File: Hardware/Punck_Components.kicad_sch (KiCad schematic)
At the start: 128 parts, among them J1 Conn_01x08_Male, J2 Conn_01x08_Male, J3 Conn_01x08_Male, J4 Conn_01x08_Male, J5 SWD_Header, J6 USB_B_Micro, J7 Eurorack_10_pin_power, Q1 MMBT3904, U1 MCP6004, U10 PCM5100APW, U11 LM2675M-5, U12 LD1117-3.3-4Tab, U2 TL074, U3 MCP6004, U5 W25Q128JVS, U6 STM32H743ZITx, U7 TL072, Y1 8MHz 20pF

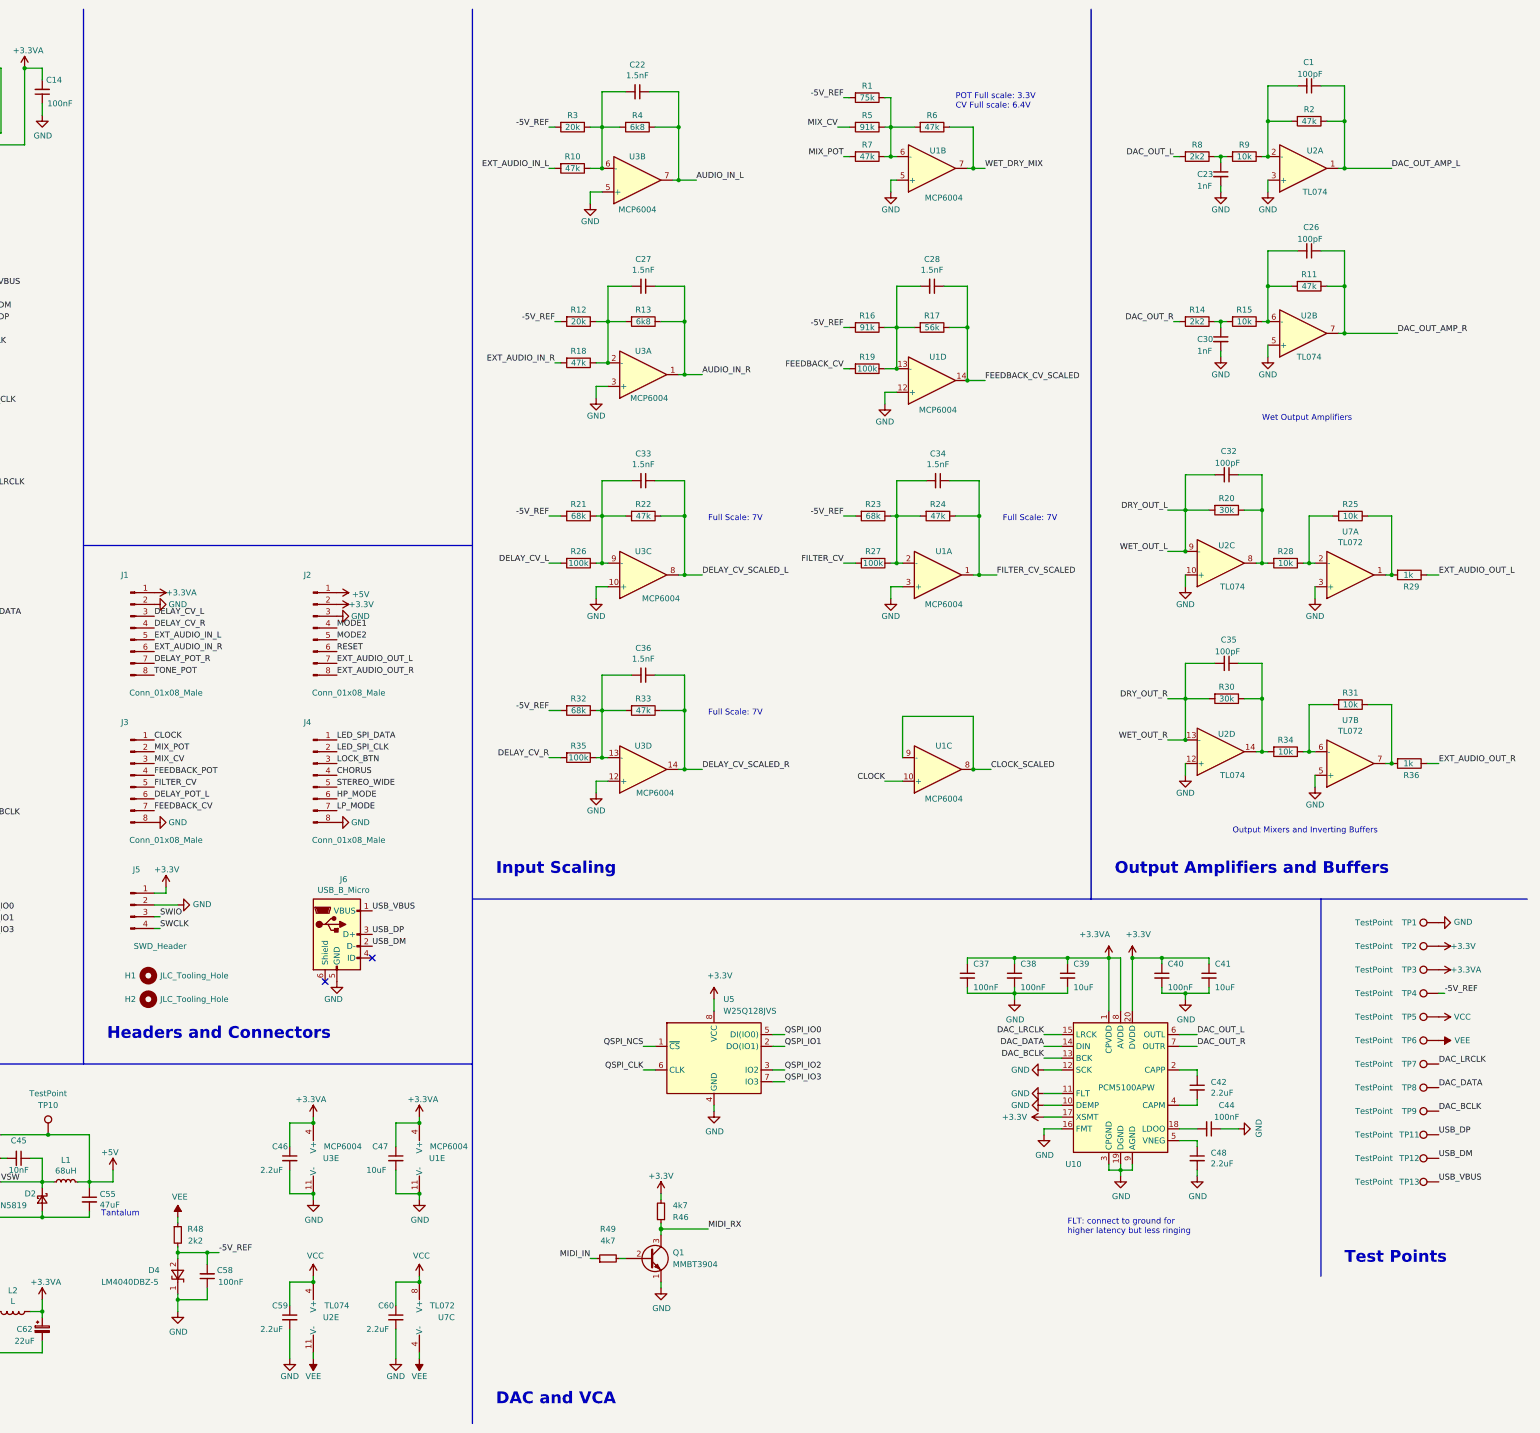
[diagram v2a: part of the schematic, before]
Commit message: Added better handling for problems with flash device
+ temporarily lowered the speed of the QSPI flash as demo rig was glitching
+ added a diagnostic to get Flash manufacturer and device ID
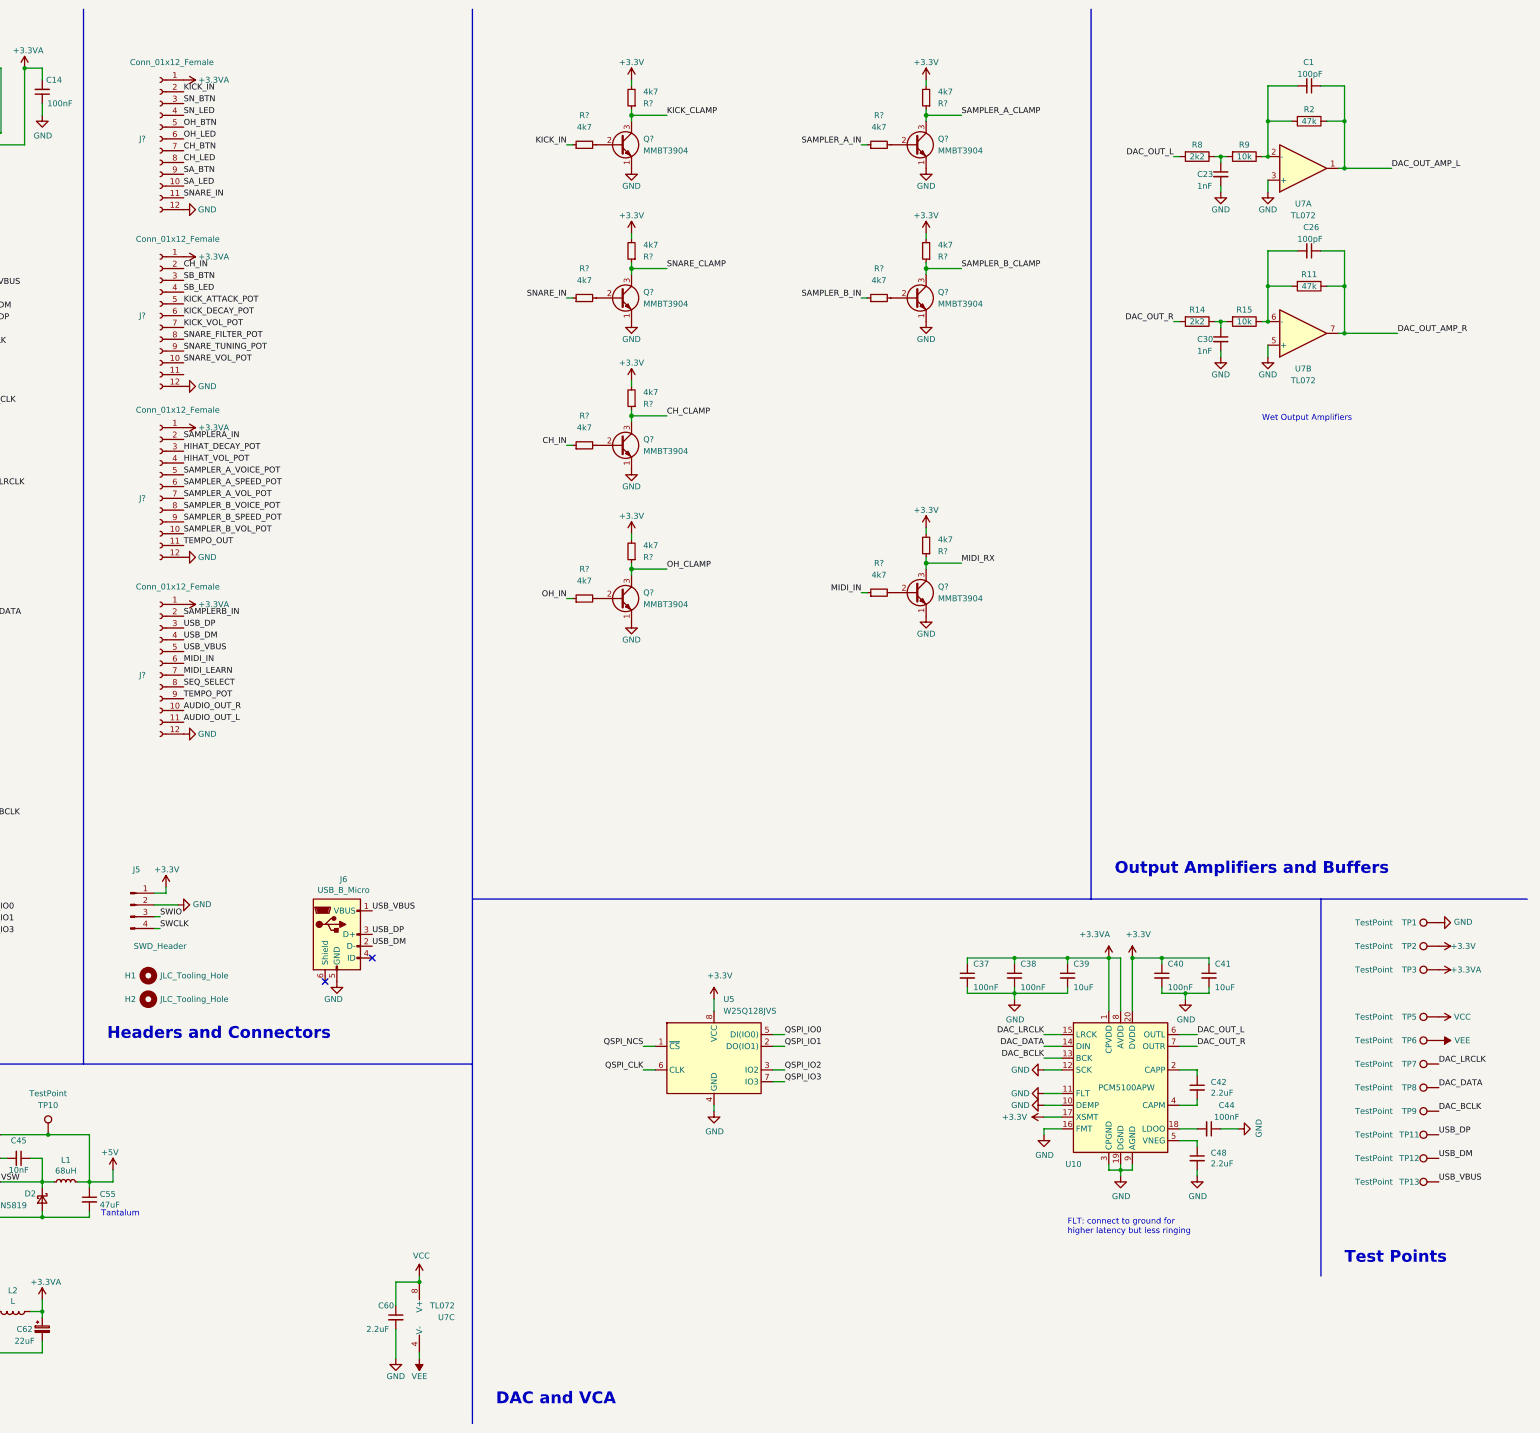
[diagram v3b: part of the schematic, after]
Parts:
- removed C22, C27, C28, C33, C34, C36: 1.5nF, Capacitors_SMD:C_0603_HandSoldering, symbol Device:C_Small
- removed C32, C35: 100pF, Capacitors_SMD:C_0603_HandSoldering, symbol Device:C_Small
- removed C46, C59: 2.2uF, Capacitors_SMD:C_0603_HandSoldering, symbol Device:C_Small
- removed C47: 10uF, Capacitors_SMD:C_0805, symbol Device:C_Small
- removed C58: 100nF, Capacitors_SMD:C_0603_HandSoldering, symbol Device:C_Small
- removed D4: LM4040DBZ-5, TO_SOT_Packages_SMD:SOT-23, symbol Reference_Voltage:LM4040DBZ-10
- removed J1, J2, J3, J4: Conn_01x08_Male, Pin_Headers:Pin_Header_Straight_1x08_Pitch2.54mm, symbol Connector:Conn_01x08_Male
- removed Q1: MMBT3904, Package_TO_SOT_THT:TO-92_Inline, symbol Transistor_BJT:2N3904
- removed R1: 75k, Resistors_SMD:R_0603_HandSoldering, symbol Device:R
- removed R10, R18, R22, R24, R33, R6, R7: 47k, Resistors_SMD:R_0603_HandSoldering, symbol Device:R
- removed R12, R3: 20k, Resistors_SMD:R_0603_HandSoldering, symbol Device:R
- removed R13, R4: 6k8, Resistors_SMD:R_0603_HandSoldering, symbol Device:R
- removed R16, R5: 91k, Resistors_SMD:R_0603_HandSoldering, symbol Device:R
- removed R17: 56k, Resistors_SMD:R_0603_HandSoldering, symbol Device:R
- removed R19, R26, R27, R35: 100k, Resistors_SMD:R_0603_HandSoldering, symbol Device:R
- removed R20, R30: 30k, Resistors_SMD:R_0603_HandSoldering, symbol Device:R
- removed R21, R23, R32: 68k, Resistors_SMD:R_0603_HandSoldering, symbol Device:R
- removed R25, R28, R31, R34: 10k, Resistors_SMD:R_0603_HandSoldering, symbol Device:R
- removed R29, R36: 1k, Resistors_SMD:R_0603_HandSoldering, symbol Device:R
- removed R46, R49: 4k7, Resistor_SMD:R_0603_1608Metric, symbol Device:R_Small
- removed R48: 2k2, Resistors_SMD:R_0603_HandSoldering, symbol Device:R_Small
- removed TP4: TestPoint, Custom_Footprints:1.3mm_Test_Point, symbol Connector:TestPoint
- removed U1, U3: MCP6004, SMD_Packages:SOIC-14_N, symbol Amplifier_Operational:MCP6004
- removed U2: TL074, SMD_Packages:SOIC-14_N, symbol Amplifier_Operational:TL074
- added J? (x4): Conn_01x12_Female, Connector_PinHeader_2.54mm:PinHeader_1x12_P2.54mm_Vertical, symbol Connector:Conn_01x12_Female
- added Q? (x7): MMBT3904, Package_TO_SOT_THT:TO-92_Inline, symbol Transistor_BJT:2N3904
- added R? (x14): 4k7, Resistor_SMD:R_0603_1608Metric, symbol Device:R_Small
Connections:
- net +3.3VA: now also J?.1 (Pin_1), J?.1 (Pin_1), J?.1 (Pin_1), J?.1 (Pin_1)
- net +3V3: now also R?.2, R?.2, R?.2, R?.2, R?.2, R?.2, R?.2
- net DAC_OUT_AMP_L: now also U7.1
- net DAC_OUT_AMP_R: now also U7.7
- net GND: now also J?.12 (Pin_12), J?.12 (Pin_12), J?.12 (Pin_12), J?.12 (Pin_12), Q?.1 (E), Q?.1 (E), Q?.1 (E), Q?.1 (E), Q?.1 (E), Q?.1 (E), Q?.1 (E)
- net MIDI_IN: now also J?.6 (Pin_6), R?.1
- net MIDI_RX: now also Q?.3 (C), R?.1
- net USB_DM: now also J?.4 (Pin_4)
- net USB_DP: now also J?.3 (Pin_3)
- net USB_VBUS: now also J?.5 (Pin_5)
- net at U7.2 (-): now also C1.2, R2.2, R9.1
- net at U7.6 (-): now also C26.2, R11.2, R15.1
- new net: Q?.2 (B), R?.2 (x7)
- new net AUDIO_OUT_L: J?.11 (Pin_11)
- new net AUDIO_OUT_R: J?.10 (Pin_10)
- new net CH_BTN: J?.7 (Pin_7)
- new net CH_CLAMP: Q?.3 (C), R?.1
- new net CH_IN: J?.2 (Pin_2), R?.1
- new net CH_LED: J?.8 (Pin_8)
- new net HIHAT_DECAY_POT: J?.3 (Pin_3)
- new net HIHAT_VOL_POT: J?.4 (Pin_4)
- new net KICK_ATTACK_POT: J?.5 (Pin_5)
- new net KICK_CLAMP: Q?.3 (C), R?.1
- new net KICK_DECAY_POT: J?.6 (Pin_6)
- new net KICK_IN: J?.2 (Pin_2), R?.1
- new net KICK_VOL_POT: J?.7 (Pin_7)
- new net MIDI_LEARN: J?.7 (Pin_7)
- new net OH_BTN: J?.5 (Pin_5)
- new net OH_CLAMP: Q?.3 (C), R?.1
- new net OH_IN: R?.1
- new net OH_LED: J?.6 (Pin_6)
- new net SAMPLERA_IN: J?.2 (Pin_2)
- new net SAMPLERB_IN: J?.2 (Pin_2)
- new net SAMPLER_A_CLAMP: Q?.3 (C), R?.1
- new net SAMPLER_A_IN: R?.1
- new net SAMPLER_A_SPEED_POT: J?.6 (Pin_6)
- new net SAMPLER_A_VOICE_POT: J?.5 (Pin_5)
- new net SAMPLER_A_VOL_POT: J?.7 (Pin_7)
- new net SAMPLER_B_CLAMP: Q?.3 (C), R?.1
- new net SAMPLER_B_IN: R?.1
- new net SAMPLER_B_SPEED_POT: J?.9 (Pin_9)
- new net SAMPLER_B_VOICE_POT: J?.8 (Pin_8)
- new net SAMPLER_B_VOL_POT: J?.10 (Pin_10)
- new net SA_BTN: J?.9 (Pin_9)
- new net SA_LED: J?.10 (Pin_10)
- new net SB_BTN: J?.3 (Pin_3)
- new net SB_LED: J?.4 (Pin_4)
- new net SEQ_SELECT: J?.8 (Pin_8)
- new net SNARE_CLAMP: Q?.3 (C), R?.1
- new net SNARE_FILTER_POT: J?.8 (Pin_8)
- new net SNARE_IN: J?.11 (Pin_11), R?.1
- new net SNARE_TUNING_POT: J?.9 (Pin_9)
- new net SNARE_VOL_POT: J?.10 (Pin_10)
- new net SN_BTN: J?.3 (Pin_3)
- new net SN_LED: J?.4 (Pin_4)
- new net TEMPO_OUT: J?.11 (Pin_11)
- new net TEMPO_POT: J?.9 (Pin_9)
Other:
- note removed: "Full Scale: 7V"
- note removed: "Input Scaling"
- note removed: "Output Mixers and Inverting Buffers"
- note removed: "POT Full scale: 3.3V CV Full scale: 6.4V"
- moved on the sheet: U7A, U7B

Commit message: Started component PCB
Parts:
- added C27, C36: (no value), symbol Device:C_Small
- added R16, R23, R24, R25, R26, R27, R28, R8: (no value), symbol Device:R_Small
- added U6: (no value), symbol Memory_Flash:W25Q128JVS
- C1: value 100pF -> (none); footprint Capacitors_SMD:C_0603_HandSoldering -> (none)
- C10, C11, C12, C13, C14, C2, C3, C4, C5, C6, C7, C8, C9: value 100nF -> (none); footprint Capacitors_SMD:C_0603_HandSoldering -> (none)
- C15: renamed from C23; value 1nF -> (none); footprint Capacitors_SMD:C_0603_HandSoldering -> (none)
- C16: renamed from C24; value 2.2uF -> (none); footprint Capacitors_SMD:C_0603_HandSoldering -> (none)
- C17: renamed from C25; value 2.2uF -> (none); footprint Capacitors_SMD:C_0603_HandSoldering -> (none)
- C18: renamed from C26; value 100pF -> (none); footprint Capacitors_SMD:C_0603_HandSoldering -> (none)
- C19: renamed from C29; value 30pF -> (none); footprint Capacitors_SMD:C_0603_HandSoldering -> (none)
- C20: renamed from C30; value 1nF -> (none); footprint Capacitors_SMD:C_0603_HandSoldering -> (none)
- C21: renamed from C31; value 30pF -> (none); footprint Capacitors_SMD:C_0603_HandSoldering -> (none)
- C22: renamed from C37; value 100nF -> (none); footprint Capacitors_SMD:C_0603_HandSoldering -> (none)
- C23: renamed from C38; value 100nF -> (none); footprint Capacitors_SMD:C_0603_HandSoldering -> (none)
- C24: renamed from C39; value 10uF -> (none); footprint Capacitors_SMD:C_0805 -> (none)
- C25: renamed from C40; value 100nF -> (none); footprint Capacitors_SMD:C_0603_HandSoldering -> (none)
- C26: renamed from C41; value 10uF -> (none); footprint Capacitors_SMD:C_0805 -> (none)
- C28: renamed from C42; value 2.2uF -> (none); footprint Capacitors_SMD:C_0603_HandSoldering -> (none)
- C29: renamed from C43; value 47uF -> (none); footprint Capacitors_SMD:CP_Elec_5x5.8 -> (none); symbol Device:CP -> Device:C_Polarized_Small
- C30: renamed from C44; value 100nF -> (none); footprint Capacitors_SMD:C_0603_HandSoldering -> (none)
- C31: renamed from C45; value 10nF -> (none); footprint Capacitors_SMD:C_0603_HandSoldering -> (none)
- C32: renamed from C48; value 2.2uF -> (none); footprint Capacitors_SMD:C_0603_HandSoldering -> (none)
- C33: renamed from C53; value 100nF -> (none); footprint Capacitors_SMD:C_0603_HandSoldering -> (none)
- C34: renamed from C54; value 22uF -> (none); footprint Capacitors_SMD:C_1210 -> (none)
- C35: renamed from C55; value 47uF -> (none); footprint Capacitors_SMD:C_1210 -> (none)
- C37: renamed from C57; value 22uF -> (none); footprint Capacitors_SMD:CP_Elec_4x5.8 -> (none); symbol Device:CP -> Device:C_Polarized_Small
- C38: renamed from C60; value 2.2uF -> (none); footprint Capacitors_SMD:C_0603_HandSoldering -> (none)
- C39: renamed from C61; value 47uF -> (none); footprint Capacitors_SMD:CP_Elec_5x5.8 -> (none); symbol Device:CP_Small -> Device:C_Polarized_Small
- C40: renamed from C62; value 22uF -> (none); footprint Capacitors_SMD:CP_Elec_4x5.8 -> (none); symbol Device:CP_Small -> Device:C_Polarized_Small
- D1, D2, D3: value 1N5819 -> (none); footprint Diodes_SMD:D_SOD-123 -> (none)
- H1, H2: value JLC_Tooling_Hole -> (none); footprint Custom_Footprints:JLC_SMT_Tooling_Hole -> (none)
- J1, J2, J3, J4: renamed from J?; value Conn_01x12_Female -> (none); footprint Connector_PinHeader_2.54mm:PinHeader_1x12_P2.54mm_Vertical -> (none)
- J5: value SWD_Header -> (none); footprint Custom_Footprints:SWD_header -> (none)
- J6: value USB_B_Micro -> (none); footprint Custom_Footprints:USB_Micro-B_Amphenol -> (none)
- J7: value Eurorack_10_pin_power -> (none); footprint Custom_Footprints:Eurorack_10_pin_header -> (none)
- L1: value 68uH -> (none); footprint Custom_Footprints:TDK_Inductor_6.9x7.2 -> (none)
- L2: value L -> (none); footprint Inductors_SMD:L_0805_HandSoldering -> (none)
- Q1, Q2, Q3, Q4, Q5, Q6, Q7: renamed from Q?; value MMBT3904 -> (none); footprint Package_TO_SOT_THT:TO-92_Inline -> (none)
- R1, R10, R12, R13, R17, R18, R19, R2, R20, R21, R22, R4, R5, R9: renamed from R?; value 4k7 -> (none); footprint Resistor_SMD:R_0603_1608Metric -> (none)
- R11: value 47k -> (none); footprint Resistors_SMD:R_0603_HandSoldering -> (none)
- R14: value 2k2 -> (none); footprint Resistors_SMD:R_0603_HandSoldering -> (none)
- R15: value 10k -> (none); footprint Resistors_SMD:R_0603_HandSoldering -> (none)
- R3: renamed from R2; value 47k -> (none); footprint Resistors_SMD:R_0603_HandSoldering -> (none)
- R6: renamed from R8; value 2k2 -> (none); footprint Resistors_SMD:R_0603_HandSoldering -> (none)
- R7: renamed from R9; value 10k -> (none); footprint Resistors_SMD:R_0603_HandSoldering -> (none)
- TP1, TP2, TP3: value TestPoint -> (none); footprint Custom_Footprints:1.3mm_Test_Point -> (none)
- TP10: renamed from TP11; value TestPoint -> (none); footprint Measurement_Points:Measurement_Point_Square-SMD-Pad_Small -> (none)
- TP11: renamed from TP12; value TestPoint -> (none); footprint Measurement_Points:Measurement_Point_Square-SMD-Pad_Small -> (none)
- TP12: renamed from TP13; value TestPoint -> (none); footprint Measurement_Points:Measurement_Point_Square-SMD-Pad_Small -> (none)
- TP4: renamed from TP5; value TestPoint -> (none); footprint Custom_Footprints:1.3mm_Test_Point -> (none)
- TP5: renamed from TP6; value TestPoint -> (none); footprint Custom_Footprints:1.3mm_Test_Point -> (none)
- TP6: renamed from TP7; value TestPoint -> (none); footprint Measurement_Points:Measurement_Point_Square-SMD-Pad_Small -> (none)
- TP7: renamed from TP8; value TestPoint -> (none); footprint Measurement_Points:Measurement_Point_Square-SMD-Pad_Small -> (none)
- TP8: renamed from TP9; value TestPoint -> (none); footprint Measurement_Points:Measurement_Point_Square-SMD-Pad_Small -> (none)
- TP9: renamed from TP10; value TestPoint -> (none); footprint Measurement_Points:Measurement_Point_Square-SMD-Pad_Small -> (none)
- U1: renamed from U7; value TL072 -> (none); footprint Housings_SOIC:SOIC-8_3.9x4.9mm_Pitch1.27mm -> (none)
- U2: renamed from U6; value STM32H743ZITx -> (none); footprint Package_QFP:LQFP-144_20x20mm_P0.5mm -> (none)
- U3: renamed from U5; value W25Q128JVS -> (none); footprint Package_SO:SOIC-8_5.23x5.23mm_P1.27mm -> (none)
- U4: renamed from U10; value PCM5100APW -> (none); footprint Custom_Footprints:SSOP-20_4.4x6.5mm_Pitch0.65mm_Round_Pads -> (none)
- U5: renamed from U11; value LM2675M-5 -> (none); footprint Housings_SOIC:SOIC-8_3.9x4.9mm_Pitch1.27mm -> (none)
- U7: renamed from U12; value LD1117-3.3-4Tab -> (none); footprint TO_SOT_Packages_SMD:SOT-223-3_TabPin2 -> (none)
- Y1: value 8MHz 20pF -> (none); footprint Crystals:Crystal_SMD_5032-2pin_5.0x3.2mm_HandSoldering -> (none)
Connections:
- net +3.3VA: no longer J2.1 (Pin_1), J3.1 (Pin_1)
- net +3V3: now also C27.1, C36.1, U6.8 (VCC)
- net AUDIO_OUT_L: now also R8.2
- net AUDIO_OUT_R: now also R16.2
- net CH_BTN: now also U2.13 (PF3)
- net CH_CLAMP: now also U2.136 (PB6)
- net CH_IN: now also J2.3 (Pin_3); no longer J2.2 (Pin_2)
- net CH_LED: now also R25.1
- net DAC_BCLK: now also U2.74 (PB13); no longer U2.117 (PD3)
- net DAC_DATA: now also U2.76 (PB15); no longer U2.29 (PC3_C)
- net GND: now also C27.2, C36.2, U6.4 (GND)
- net HIHAT_DECAY_POT: now also U2.46 (PB0)
- net HIHAT_VOL_POT: now also U2.47 (PB1)
- net KICK_ATTACK_POT: now also J2.6 (Pin_6), U2.34 (PA0); no longer J2.5 (Pin_5)
- net KICK_CLAMP: now also U2.137 (PB7)
- net KICK_DECAY_POT: now also J2.7 (Pin_7), U2.35 (PA1); no longer J2.6 (Pin_6)
- net KICK_VOL_POT: now also J2.8 (Pin_8), U2.36 (PA2); no longer J2.7 (Pin_7)
- net MIDI_LEARN: now also U2.67 (PE14)
- net OH_BTN: now also U2.12 (PF2)
- net OH_CLAMP: now also U2.93 (PG8)
- net OH_IN: now also J3.1 (Pin_1)
- net OH_LED: now also R26.1
- net QSPI_CLK: now also U6.6 (CLK)
- net QSPI_IO2: no longer U3.3 (IO2)
- net SAMPLER_A_CLAMP: now also U2.125 (PG10)
- net SAMPLER_A_SPEED_POT: now also U2.27 (PC1)
- net SAMPLER_A_VOICE_POT: now also U2.26 (PC0)
- net SAMPLER_A_VOL_POT: now also U2.44 (PC4)
- net SAMPLER_B_CLAMP: now also U2.128 (PG13)
- net SAMPLER_B_SPEED_POT: now also U2.49 (PF11)
- net SAMPLER_B_VOICE_POT: now also U2.45 (PC5)
- net SAMPLER_B_VOL_POT: now also U2.50 (PF12)
- net SA_BTN: now also U2.14 (PF4)
- net SA_LED: now also R27.1
- net SB_BTN: now also J2.4 (Pin_4), U2.15 (PF5); no longer J2.3 (Pin_3)
- net SB_LED: now also J2.5 (Pin_5), R28.1; no longer J2.4 (Pin_4)
- net SEQ_SELECT: now also U2.68 (PE15)
- net SNARE_CLAMP: now also U2.135 (PB5)
- net SNARE_FILTER_POT: now also J2.9 (Pin_9), U2.37 (PA3); no longer J2.8 (Pin_8)
- net SNARE_TUNING_POT: now also J2.10 (Pin_10), U2.42 (PA6); no longer J2.9 (Pin_9)
- net SNARE_VOL_POT: now also J2.11 (Pin_11), U2.43 (PA7); no longer J2.10 (Pin_10)
- net SN_BTN: now also U2.11 (PF1)
- net SN_LED: now also R24.1
- net TEMPO_OUT: now also U2.134 (PB4)
- net TEMPO_POT: now also U2.53 (PF13)
- net KI_BTN: now reaches U2.10 (PF0)
- net KI_BTN: now also J2.1 (Pin_1)
- net QSPI_BK2_NCS: now reaches U2.112 (PC11)
- net QSPI_BK2_NCS: now also U6.1 (~{CS})
- net QSPI_BK2_IO0: now reaches U2.58 (PE7)
- net QSPI_BK2_IO0: now also U6.5 (DI(IO0))
- net QSPI_BK2_IO1: now reaches U2.59 (PE8)
- net QSPI_BK2_IO1: now also U6.2 (DO(IO1))
- net QSPI_BK2_IO2: now reaches U2.60 (PE9)
- net QSPI_BK2_IO2: now also U6.3 (IO2)
- net QSPI_BK2_IO3: now reaches U2.63 (PE10)
- net QSPI_BK2_IO3: now also U6.7 (IO3)
- net SA_LED_OUT: now reaches U2.85 (PD14)
- net SA_LED_OUT: now also R27.2
- net SB_LED_OUT: now reaches U2.86 (PD15)
- net SB_LED_OUT: now also R28.2
- net KI_LED_OUT: now reaches U2.96 (PC6)
- net KI_LED_OUT: now also R23.2
- net SN_LED_OUT: now reaches U2.97 (PC7)
- net SN_LED_OUT: now also R24.2
- net CH_LED_OUT: now reaches U2.98 (PC8)
- net CH_LED_OUT: now also R25.2
- net OH_LED_OUT: now reaches U2.99 (PC9)
- net OH_LED_OUT: now also R26.2
- net DAC_OUT_AMP_L: no longer names the net of C1.1, R3.1, U1.1
- net DAC_OUT_AMP_L: now also R8.1
- net DAC_OUT_AMP_R: no longer names the net of C18.1, R11.1, U1.7
- net DAC_OUT_AMP_R: now also R16.1
- net QSPI_IO0 renamed QSPI_BK1_IO0
- net QSPI_IO1 renamed QSPI_BK1_IO1
- net QSPI_IO3 renamed QSPI_BK1_IO3
- net QSPI_NCS renamed QSPI_BK1_NCS
- new net KI_LED: J2.2 (Pin_2), R23.1
- new net QSPI_BK1_IO2: U3.3 (IO2)
- no-connect marks 39 -> 57
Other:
- note added: "ADC Pins -------- PA0 ADC1_INP16 PA1 ADC1_INP17 PA2 ADC12_INP14 PA3 ADC12_INP15 [PA4 ADC12_INP18 DAC] [PA5 ADC12_INP19 DAC] PA6 ADC12_INP3 PA7 ADC12_INP7 PB0 ADC12_INP9 PB1 ADC12_INP5 PC0 ADC123_INP10 PC1 ADC123_INP11 PC2 ADC123_INP12 [PC3_C ADC3_INP1] PC4 ADC12_INP4 PC5 ADC12_INP8 PF11 ADC1_INP2 PF12 ADC1_INP6 PF13 ADC2_INP2 PF14 ADC2_INP6"
- note added: "Flash"
- note added: "LED Pins -------- PC6-9: TIM3/TIM8 PD12-15: TIM4 PB4-5: TIM3 PB6-7: TIM4"
- note added: "Other Test connectors: DAC UART ADC MISC IO"
- note removed: "DAC and VCA"
- moved on the sheet: C38, U1C
